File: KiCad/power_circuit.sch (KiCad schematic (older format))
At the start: 15 parts

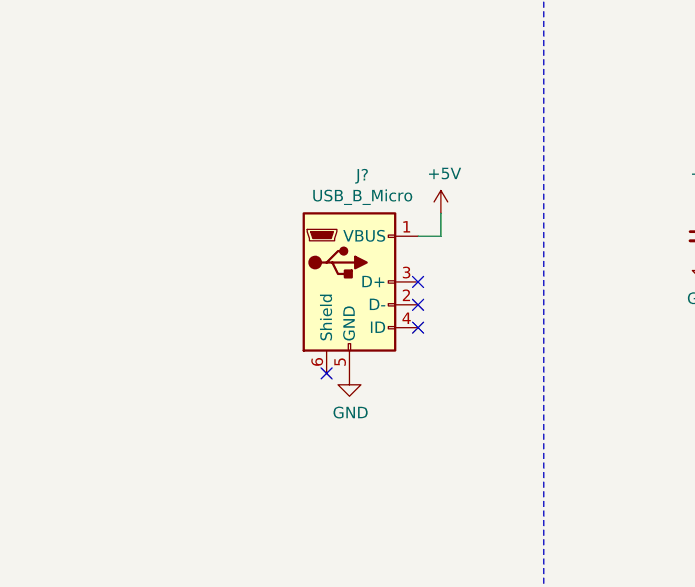
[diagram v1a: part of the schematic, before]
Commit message: added green LED for when USB is connected to power circuit
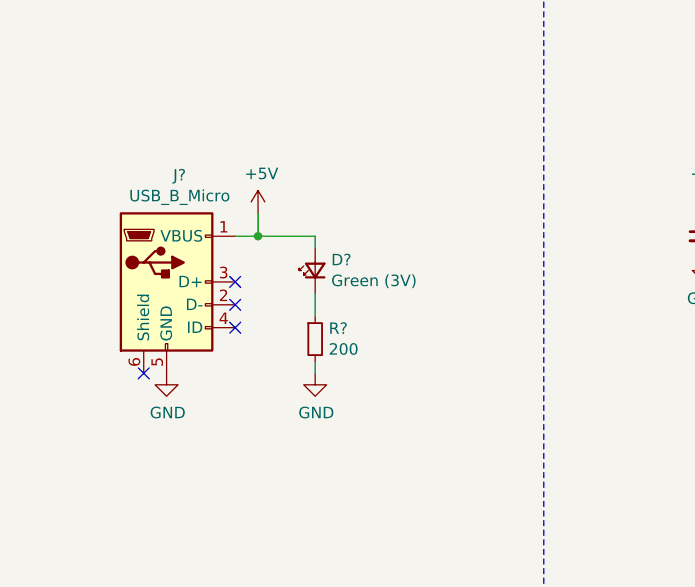
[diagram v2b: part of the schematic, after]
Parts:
- added D?: Green (3V), symbol Device:LED_Small
- added R?: 200, symbol Device:R_Small
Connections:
- net +5V: now also D?.2 (A)
- net GND: now also R?.2
- new net: D?.1 (K), R?.1
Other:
- moved on the sheet: J?
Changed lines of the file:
@@
 L Connector:USB_B_Micro J?
 U 1 1 60920846
-P 1950 3050
-F 0 "J?" H 2007 3517 50  0000 C CNN
-F 1 "USB_B_Micro" H 2007 3426 50  0000 C CNN
-F 2 "" H 2100 3000 50  0001 C CNN
-F 3 "~" H 2100 3000 50  0001 C CNN
-	1    1950 3050
+P 1150 3050
+F 0 "J?" H 1207 3517 50  0000 C CNN
+F 1 "USB_B_Micro" H 1207 3426 50  0000 C CNN
+F 2 "" H 1300 3000 50  0001 C CNN
+F 3 "~" H 1300 3000 50  0001 C CNN
+	1    1150 3050
 	1    0    0    -1
 $EndComp
@@
 L power:+5V #PWR?
 U 1 1 60922D22
-P 2350 2750
-F 0 "#PWR?" H 2350 2600 50  0001 C CNN
-F 1 "+5V" H 2365 2923 50  0000 C CNN
-F 2 "" H 2350 2750 50  0001 C CNN
-F 3 "" H 2350 2750 50  0001 C CNN
-	1    2350 2750
-	1    0    0    -1
-$EndComp
-Wire Wire Line
-	2350 2750 2350 2850
-Wire Wire Line
-	2350 2850 2250 2850
-NoConn ~ 1850 3450
+P 1550 2750
+F 0 "#PWR?" H 1550 2600 50  0001 C CNN
+F 1 "+5V" H 1565 2923 50  0000 C CNN
+F 2 "" H 1550 2750 50  0001 C CNN
+F 3 "" H 1550 2750 50  0001 C CNN
+	1    1550 2750
+	1    0    0    -1
+$EndComp
+Wire Wire Line
+	1550 2750 1550 2850
+Wire Wire Line
+	1550 2850 1450 2850
+NoConn ~ 1050 3450
 $Comp
 L power:GND #PWR?
 U 1 1 6092662F
-P 1950 3450
-F 0 "#PWR?" H 1950 3200 50  0001 C CNN
-F 1 "GND" H 1955 3277 50  0000 C CNN
-F 2 "" H 1950 3450 50  0001 C CNN
-F 3 "" H 1950 3450 50  0001 C CNN
-	1    1950 3450
-	1    0    0    -1
-$EndComp
-NoConn ~ 2250 3050
-NoConn ~ 2250 3150
-NoConn ~ 2250 3250
+P 1150 3450
+F 0 "#PWR?" H 1150 3200 50  0001 C CNN
+F 1 "GND" H 1155 3277 50  0000 C CNN
+F 2 "" H 1150 3450 50  0001 C CNN
+F 3 "" H 1150 3450 50  0001 C CNN
+	1    1150 3450
+	1    0    0    -1
+$EndComp
+NoConn ~ 1450 3050
+NoConn ~ 1450 3150
+NoConn ~ 1450 3250
 $Comp
 L Device:C_Small C?
@@
 Text Notes 7750 1650 0    50   ~ 0
 Buck converter to power all the other circtuits
+$Comp
+L Device:LED_Small D?
+U 1 1 609BC12A
+P 1800 3000
+F 0 "D?" V 1846 2930 50  0000 R CNN
+F 1 "Green (3V)" V 1755 2930 50  0000 R CNN
+F 2 "" V 1800 3000 50  0001 C CNN
+F 3 "~" V 1800 3000 50  0001 C CNN
+	1    1800 3000
+	0    -1   -1   0
+$EndComp
+$Comp
+L Device:R_Small R?
+U 1 1 609BE181
+P 1800 3300
+F 0 "R?" H 1859 3346 50  0000 L CNN
+F 1 "200" H 1859 3255 50  0000 L CNN
+F 2 "" H 1800 3300 50  0001 C CNN
+F 3 "~" H 1800 3300 50  0001 C CNN
+	1    1800 3300
+	1    0    0    -1
+$EndComp
+Wire Wire Line
+	1800 3100 1800 3200
+Wire Wire Line
+	1800 2900 1800 2850
+Wire Wire Line
+	1800 2850 1550 2850
+Connection ~ 1550 2850
+$Comp
+L power:GND #PWR?
+U 1 1 609C1818
+P 1800 3450
+F 0 "#PWR?" H 1800 3200 50  0001 C CNN
+F 1 "GND" H 1805 3277 50  0000 C CNN
+F 2 "" H 1800 3450 50  0001 C CNN
+F 3 "" H 1800 3450 50  0001 C CNN
+	1    1800 3450
+	1    0    0    -1
+$EndComp
+Wire Wire Line
+	1800 3450 1800 3400
 $EndSCHEMATC

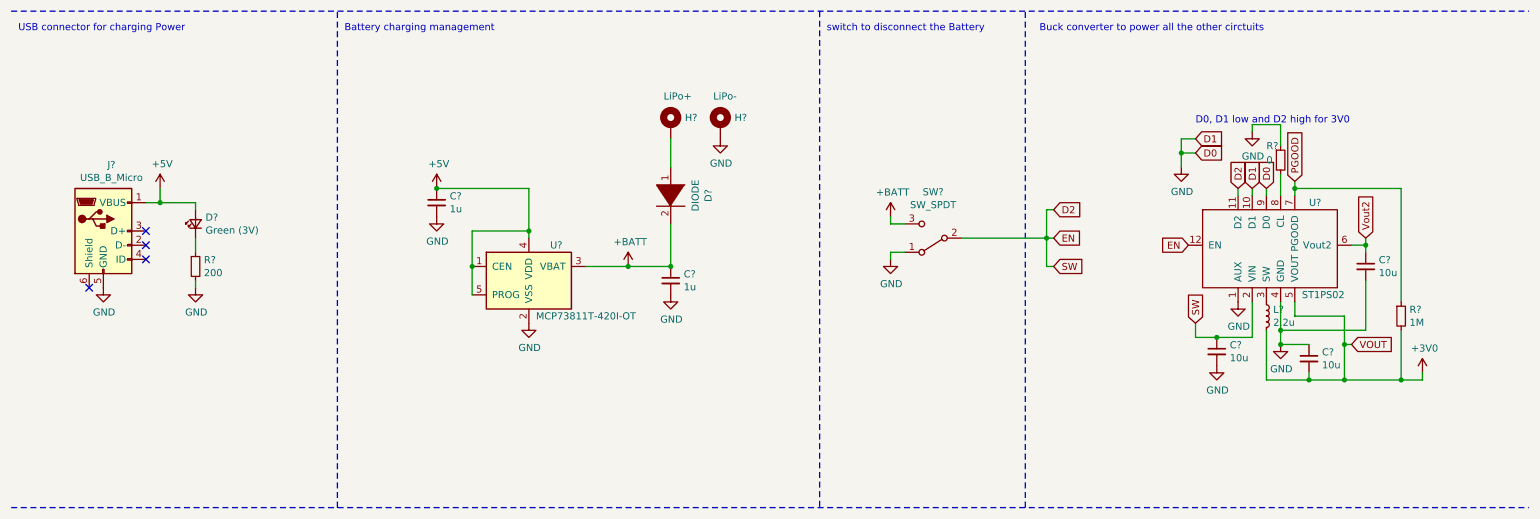
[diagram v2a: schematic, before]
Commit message: added battery voltage supervision version 1
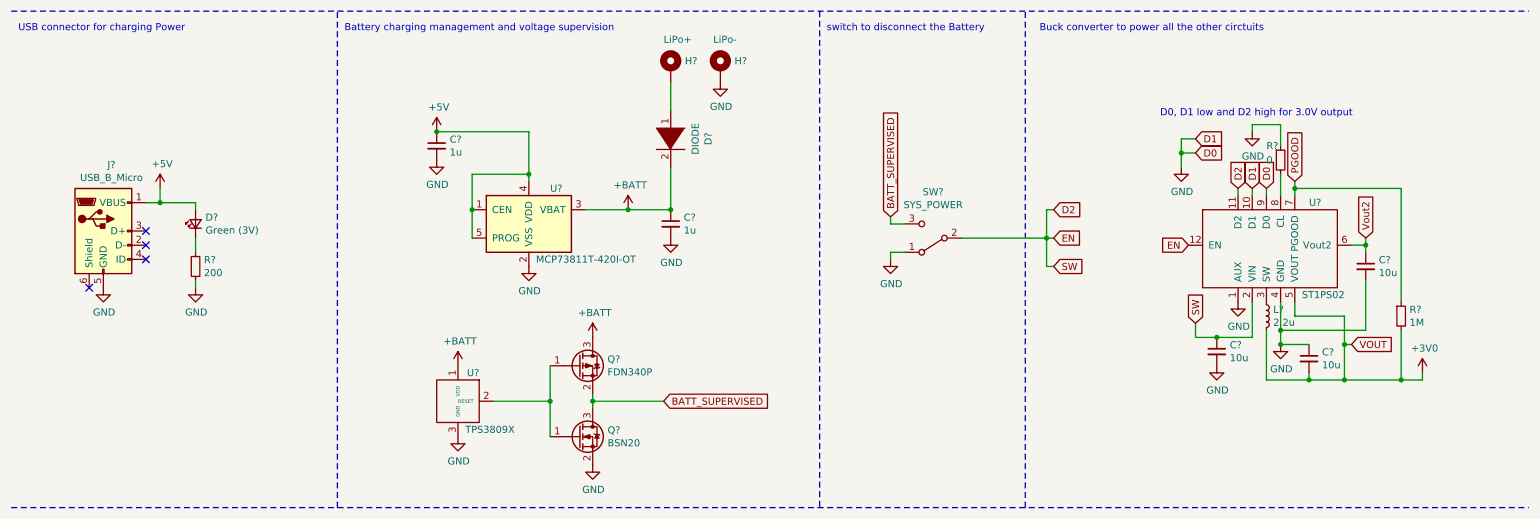
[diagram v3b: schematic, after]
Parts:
- added Q?: FDN340P, Package_TO_SOT_SMD:SOT-23, symbol Transistor_FET:FDN340P
- added Q?: BSN20, Package_TO_SOT_SMD:SOT-23, symbol Transistor_FET:BSN20
- added U?: TPS3809X, symbol Nils_KiCADLibrary:TPS3809X
- SW?: value SW_SPDT -> SYS_POWER
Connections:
- net +BATT: now also Q?.3 (D), U?.1 (VDD); no longer SW?.3 (C)
- net GND: now also Q?.2 (S), U?.3 (GND)
- new net: Q?.1 (G), Q?.1 (G), U?.2 (RESET)
- new net BATT_SUPERVISED: Q?.2 (S), Q?.3 (D), SW?.3 (C)
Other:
- note added: "Battery charging management and voltage supervision"
- note added: "D0, D1 low and D2 high for 3.0V output"
- note removed: "Battery charging management"
- note removed: "D0, D1 low and D2 high for 3V0"
- moved on the sheet: C?, D?, H?, U?

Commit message: corrected battery voltage supervision
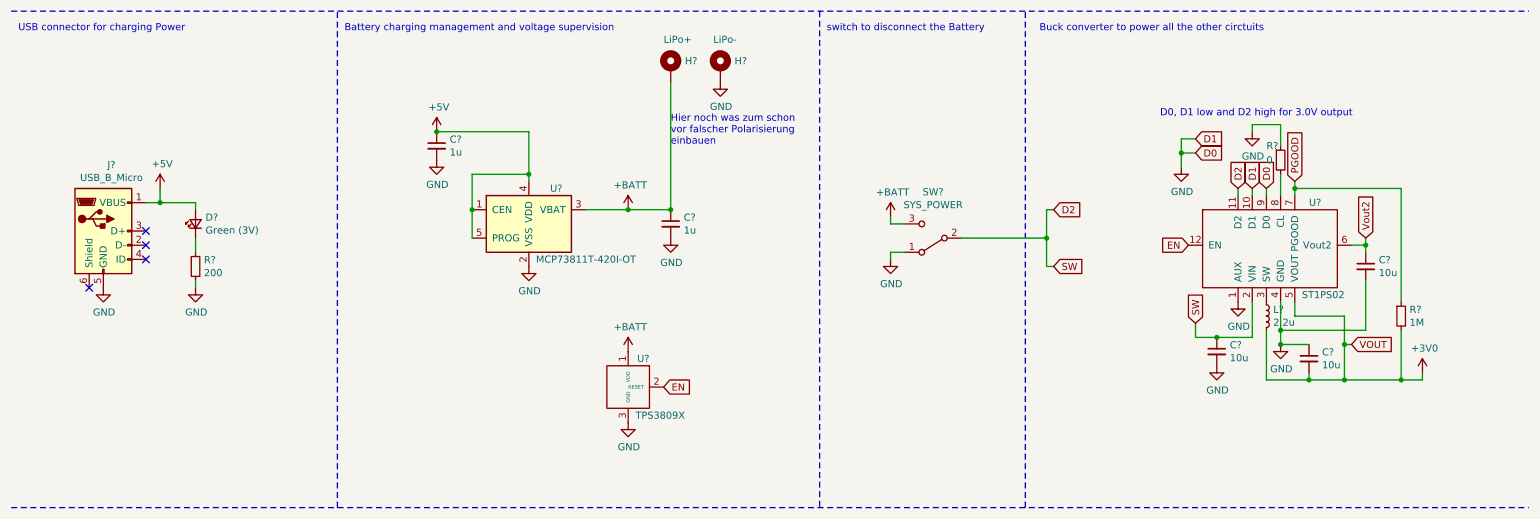
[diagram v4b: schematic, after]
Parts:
- removed D?: DIODE, symbol pspice:DIODE
- removed Q?: FDN340P, Package_TO_SOT_SMD:SOT-23, symbol Transistor_FET:FDN340P
- removed Q?: BSN20, Package_TO_SOT_SMD:SOT-23, symbol Transistor_FET:BSN20
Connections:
- net BATT_SUPERVISED is gone; now on net +BATT: SW?.3 (C)
- net +BATT: now also H?.1
- net D2: no longer U?.12 (EN)
- net EN: now reaches U?.2 (RESET)
- net EN: now also U?.12 (EN)
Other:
- note added: "Hier noch was zum schon\nvor falscher Polarisierung\neinbauen"
- moved on the sheet: U?
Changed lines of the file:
@@
 	7800 3100 7800 3300
-Wire Wire Line
-	7800 3100 7850 3100
 Wire Wire Line
 	7800 2900 7850 2900
@@
 Text GLabel 7850 3300 2    50   Input ~ 0
 SW
-$Comp
-L pspice:DIODE D?
-U 1 1 6091BD94
-P 5150 2400
-AR Path="/6091BD94" Ref="D?"  Part="1"
-AR Path="/608A57BF/6091BD94" Ref="D?"  Part="1"
-F 0 "D?" H 5150 2665 50  0000 C CNN
-F 1 "DIODE" H 5150 2574 50  0000 C CNN
-F 2 "" H 5150 2400 50  0001 C CNN
-F 3 "~" H 5150 2400 50  0001 C CNN
-	1    5150 2400
-	0    1    1    0
-$EndComp
-Text GLabel 7850 3100 2    50   Input ~ 0
-EN
 $Comp
 L Switch:SW_SPDT SW?
@@
 Wire Wire Line
 	4850 2900 5150 2900
-Wire Wire Line
-	5150 2600 5150 2900
 Connection ~ 5150 2900
-Wire Wire Line
-	5150 2200 5150 2000
 Wire Notes Line
 	500  1500 11200 1500
@@
 L Nils_KiCADLibrary:TPS3809X U?
 U 1 1 609D9E73
-P 3650 4250
-F 0 "U?" H 3800 4450 50  0000 R CNN
-F 1 "TPS3809X" H 4050 4050 50  0000 R CNN
-F 2 "" H 3650 4200 50  0001 C CNN
-F 3 "" H 3650 4200 50  0001 C CNN
-	1    3650 4250
-	1    0    0    -1
-$EndComp
-Text GLabel 5100 4250 2    50   Input ~ 0
-BATT_SUPERVISED
-Text GLabel 6700 2950 1    50   Input ~ 0
-BATT_SUPERVISED
+P 4850 4150
+F 0 "U?" H 5000 4350 50  0000 R CNN
+F 1 "TPS3809X" H 5250 3950 50  0000 R CNN
+F 2 "" H 4850 4100 50  0001 C CNN
+F 3 "" H 4850 4100 50  0001 C CNN
+	1    4850 4150
+	1    0    0    -1
+$EndComp
 $Comp
 L power:+BATT #PWR?
 U 1 1 609F1C8D
-P 3650 4000
+P 4850 3900
 AR Path="/609F1C8D" Ref="#PWR?"  Part="1"
 AR Path="/608A57BF/609F1C8D" Ref="#PWR?"  Part="1"
-F 0 "#PWR?" H 3650 3850 50  0001 C CNN
-F 1 "+BATT" H 3665 4173 50  0000 C CNN
-F 2 "" H 3650 4000 50  0001 C CNN
-F 3 "" H 3650 4000 50  0001 C CNN
-	1    3650 4000
+F 0 "#PWR?" H 4850 3750 50  0001 C CNN
+F 1 "+BATT" H 4865 4073 50  0000 C CNN
+F 2 "" H 4850 3900 50  0001 C CNN
+F 3 "" H 4850 3900 50  0001 C CNN
+	1    4850 3900
 	1    0    0    -1
 $EndComp
@@
 L power:GND #PWR?
 U 1 1 609F4A79
-P 3650 4500
-F 0 "#PWR?" H 3650 4250 50  0001 C CNN
-F 1 "GND" H 3655 4327 50  0000 C CNN
-F 2 "" H 3650 4500 50  0001 C CNN
-F 3 "" H 3650 4500 50  0001 C CNN
-	1    3650 4500
+P 4850 4400
+F 0 "#PWR?" H 4850 4150 50  0001 C CNN
+F 1 "GND" H 4855 4227 50  0000 C CNN
+F 2 "" H 4850 4400 50  0001 C CNN
+F 3 "" H 4850 4400 50  0001 C CNN
+	1    4850 4400
 	1    0    0    -1
 $EndComp
 Wire Notes Line
 	500  5000 11200 5000
+Wire Wire Line
+	5150 2000 5150 2900
+Text Notes 5150 2450 0    50   ~ 0
+Hier noch was zum schon\nvor falscher Polarisierung\neinbauen
+Text GLabel 5100 4150 2    50   Input ~ 0
+EN
 $Comp
 L power:+BATT #PWR?
-U 1 1 60A23FBC
-P 4600 3800
-AR Path="/60A23FBC" Ref="#PWR?"  Part="1"
-AR Path="/608A57BF/60A23FBC" Ref="#PWR?"  Part="1"
-F 0 "#PWR?" H 4600 3650 50  0001 C CNN
-F 1 "+BATT" H 4615 3973 50  0000 C CNN
-F 2 "" H 4600 3800 50  0001 C CNN
-F 3 "" H 4600 3800 50  0001 C CNN
-	1    4600 3800
-	1    0    0    -1
-$EndComp
-$Comp
-L power:GND #PWR?
-U 1 1 60A2835B
-P 4600 4700
-F 0 "#PWR?" H 4600 4450 50  0001 C CNN
-F 1 "GND" H 4605 4527 50  0000 C CNN
-F 2 "" H 4600 4700 50  0001 C CNN
-F 3 "" H 4600 4700 50  0001 C CNN
-	1    4600 4700
-	1    0    0    -1
-$EndComp
-$Comp
-L Transistor_FET:FDN340P Q?
-U 1 1 60A31F43
-P 4500 4000
-F 0 "Q?" H 4704 4046 50  0000 L CNN
-F 1 "FDN340P" H 4704 3955 50  0000 L CNN
-F 2 "Package_TO_SOT_SMD:SOT-23" H 4700 3925 50  0001 L CIN
-F 3 "https://www.onsemi.com/pub/Collateral/FDN340P-D.PDF" H 4500 4000 50  0001 L CNN
-	1    4500 4000
-	1    0    0    -1
-$EndComp
-$Comp
-L Transistor_FET:BSN20 Q?
-U 1 1 60A332F7
-P 4500 4500
-F 0 "Q?" H 4705 4546 50  0000 L CNN
-F 1 "BSN20" H 4705 4455 50  0000 L CNN
-F 2 "Package_TO_SOT_SMD:SOT-23" H 4700 4425 50  0001 L CIN
-F 3 "http://www.diodes.com/assets/Datasheets/ds31898.pdf" H 4500 4500 50  0001 L CNN
-	1    4500 4500
-	1    0    0    -1
-$EndComp
-Wire Wire Line
-	3900 4250 4300 4250
-Wire Wire Line
-	4300 4250 4300 4000
-Wire Wire Line
-	4300 4250 4300 4500
-Connection ~ 4300 4250
-Wire Wire Line
-	4600 4200 4600 4250
-Wire Wire Line
-	4600 4250 5100 4250
-Connection ~ 4600 4250
-Wire Wire Line
-	4600 4250 4600 4300
+U 1 1 608829DA
+P 6700 2950
+AR Path="/608829DA" Ref="#PWR?"  Part="1"
+AR Path="/608A57BF/608829DA" Ref="#PWR?"  Part="1"
+F 0 "#PWR?" H 6700 2800 50  0001 C CNN
+F 1 "+BATT" H 6715 3123 50  0000 C CNN
+F 2 "" H 6700 2950 50  0001 C CNN
+F 3 "" H 6700 2950 50  0001 C CNN
+	1    6700 2950
+	1    0    0    -1
+$EndComp
 $EndSCHEMATC

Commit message: paar Kommentare/Ideen zur voltage supervision hinzugefügt
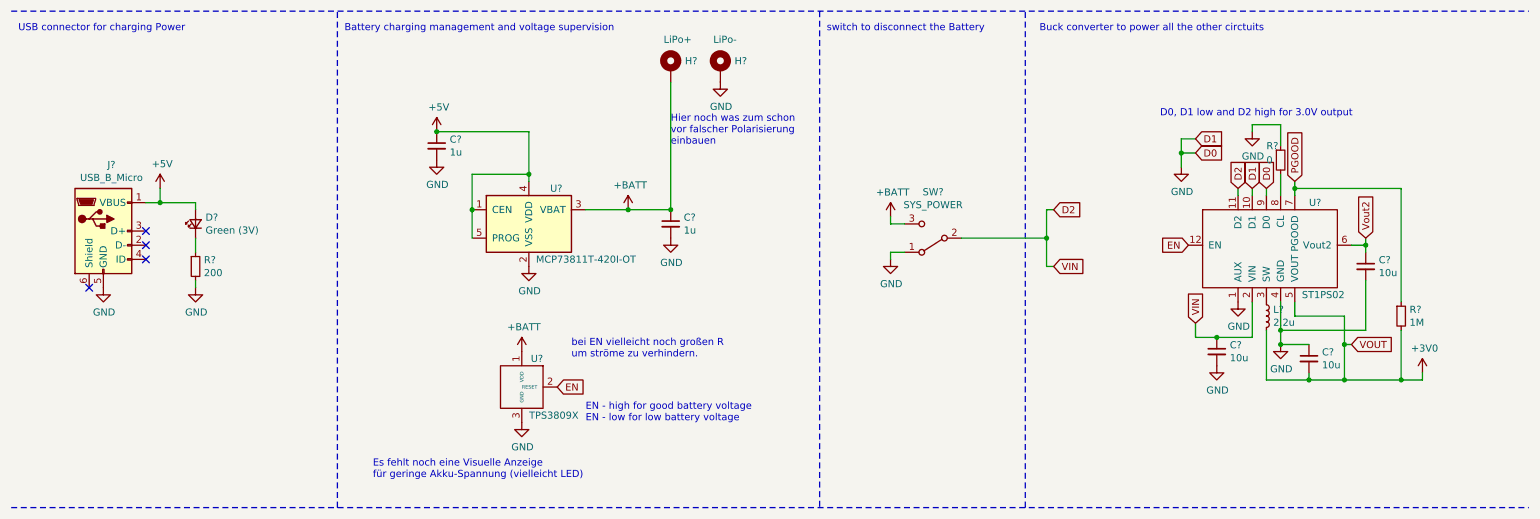
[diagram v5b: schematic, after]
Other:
- note added: "EN - high for good battery voltage\nEN - low for low battery voltage"
- note added: "Es fehlt noch eine Visuelle Anzeige\nfür geringe Akku-Spannung (vielleicht LED)"
- note added: "bei EN vielleicht noch großen R\num ströme zu verhindern."
- moved on the sheet: U?
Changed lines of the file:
@@
 	9150 2800 9150 2750
 Text GLabel 8850 3700 1    50   Input ~ 0
-SW
+VIN
 Text GLabel 8850 2500 2    50   Input ~ 0
 D0
@@
 D2
 Text GLabel 7850 3300 2    50   Input ~ 0
-SW
+VIN
 $Comp
 L Switch:SW_SPDT SW?
@@
 L Nils_KiCADLibrary:TPS3809X U?
 U 1 1 609D9E73
-P 4850 4150
-F 0 "U?" H 5000 4350 50  0000 R CNN
-F 1 "TPS3809X" H 5250 3950 50  0000 R CNN
-F 2 "" H 4850 4100 50  0001 C CNN
-F 3 "" H 4850 4100 50  0001 C CNN
-	1    4850 4150
+P 4100 4150
+F 0 "U?" H 4250 4350 50  0000 R CNN
+F 1 "TPS3809X" H 4500 3950 50  0000 R CNN
+F 2 "" H 4100 4100 50  0001 C CNN
+F 3 "" H 4100 4100 50  0001 C CNN
+	1    4100 4150
 	1    0    0    -1
 $EndComp
@@
 L power:+BATT #PWR?
 U 1 1 609F1C8D
-P 4850 3900
+P 4100 3900
 AR Path="/609F1C8D" Ref="#PWR?"  Part="1"
 AR Path="/608A57BF/609F1C8D" Ref="#PWR?"  Part="1"
-F 0 "#PWR?" H 4850 3750 50  0001 C CNN
-F 1 "+BATT" H 4865 4073 50  0000 C CNN
-F 2 "" H 4850 3900 50  0001 C CNN
-F 3 "" H 4850 3900 50  0001 C CNN
-	1    4850 3900
+F 0 "#PWR?" H 4100 3750 50  0001 C CNN
+F 1 "+BATT" H 4115 4073 50  0000 C CNN
+F 2 "" H 4100 3900 50  0001 C CNN
+F 3 "" H 4100 3900 50  0001 C CNN
+	1    4100 3900
 	1    0    0    -1
 $EndComp
@@
 L power:GND #PWR?
 U 1 1 609F4A79
-P 4850 4400
-F 0 "#PWR?" H 4850 4150 50  0001 C CNN
-F 1 "GND" H 4855 4227 50  0000 C CNN
-F 2 "" H 4850 4400 50  0001 C CNN
-F 3 "" H 4850 4400 50  0001 C CNN
-	1    4850 4400
+P 4100 4400
+F 0 "#PWR?" H 4100 4150 50  0001 C CNN
+F 1 "GND" H 4105 4227 50  0000 C CNN
+F 2 "" H 4100 4400 50  0001 C CNN
+F 3 "" H 4100 4400 50  0001 C CNN
+	1    4100 4400
 	1    0    0    -1
 $EndComp
@@
 Text Notes 5150 2450 0    50   ~ 0
 Hier noch was zum schon\nvor falscher Polarisierung\neinbauen
-Text GLabel 5100 4150 2    50   Input ~ 0
+Text GLabel 4350 4150 2    50   Input ~ 0
 EN
 $Comp
@@
 	1    0    0    -1
 $EndComp
+Text Notes 4550 4400 0    50   ~ 0
+EN - high for good battery voltage\nEN - low for low battery voltage
+Text Notes 3050 4800 0    50   ~ 0
+Es fehlt noch eine Visuelle Anzeige\nfür geringe Akku-Spannung (vielleicht LED)
+Text Notes 4450 3950 0    50   ~ 0
+bei EN vielleicht noch großen R\num ströme zu verhindern.
 $EndSCHEMATC
